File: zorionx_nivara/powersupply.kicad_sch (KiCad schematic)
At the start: 6 parts, among them U2 AP63203WU

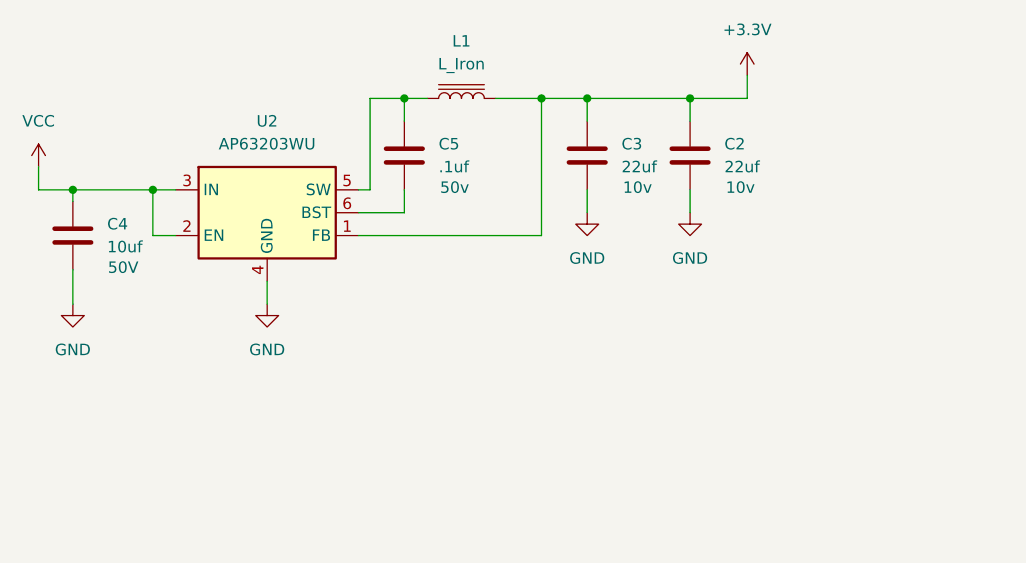
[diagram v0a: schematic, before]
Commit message: ruteo power
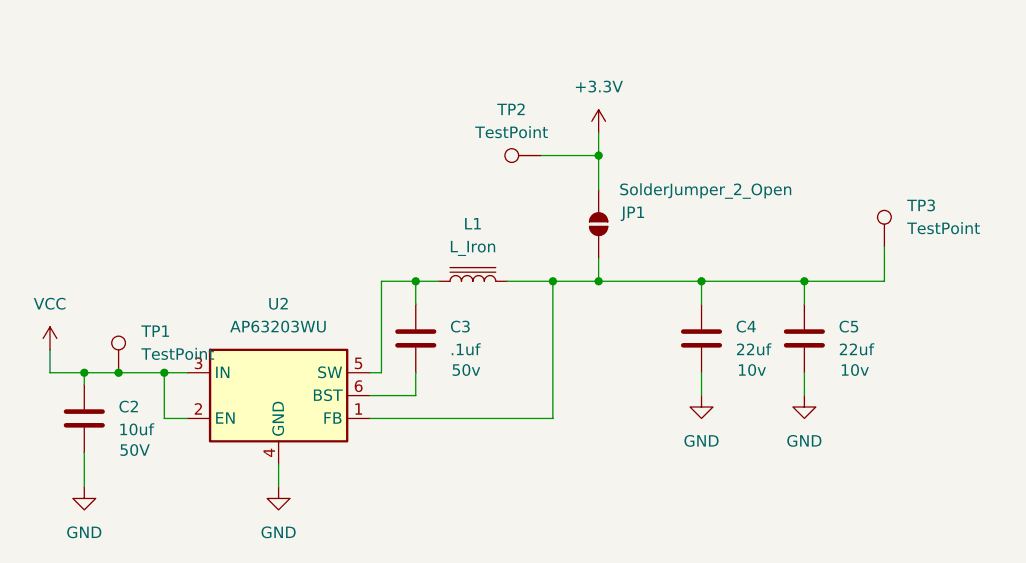
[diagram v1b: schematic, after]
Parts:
- added JP1: SolderJumper_2_Open, Jumper:SolderJumper-2_P1.3mm_Open_RoundedPad1.0x1.5mm, symbol Jumper:SolderJumper_2_Open
- added TP1, TP2, TP3: TestPoint, TestPoint:TestPoint_Loop_D1.80mm_Drill1.0mm_Beaded, symbol Connector:TestPoint
- renumbered C4 to C2, C5 to C3, C3 to C4, C2 to C5
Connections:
- net +3.3V: now also JP1.2 (B), TP2.1; no longer C4.1, C5.1, L1.2, U2.1 (FB)
- net VCC: now also TP1.1
- new net: C4.1, C5.1, JP1.1 (A), L1.2, TP3.1, U2.1 (FB)
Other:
- moved on the sheet: C2, C3, C4, C5, L1, U2
